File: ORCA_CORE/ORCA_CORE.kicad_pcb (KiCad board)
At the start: 4 copper layers, 73 x 134.1 mm, 184 parts, among them J1 data_line_power, J10 Raspberry_Pi_2_3, J11 I2C, J12 I2C, J13 6Vout, J15 Conn_01x05_Pin, J16 Conn_01x05_Pin, J17 Vin_motor, J18 data_line_power, J19 +5Vin_cpu, J2 I2C_power, J20 5Vout, J21 Conn_01x02, J3 Vout_motor, J4 emergence, J5 Vin_batt, J6 Vin_ex, J7 Vout_power2usp, J8 Vin_power2usp, J9 +5Vout_cpu, P1 USB_C_Receptacle_USB2.0, Q1 TJ60S04M3L, Q2 BSS138, Q3 BSS138, Q4 IRLML6402, Q5 TJ60S04M3L, Q6 BSS138, Q7 BSS138, Q8 BSS138, U1 LTC2301IMS, U10 HY2112, U11 AP64502, U12 TPS61230A__board, U13 FT230XS, U14 BNO055, U15 NJM78055DL1, U2 NJM78055DL1, U3 CN3058E, U4 RH1B-UDC6V, U5 TPH11006NL, U6 TPH11006NL, U7 NJW4860, U8 AZ1117-3.3, U9 FS8205

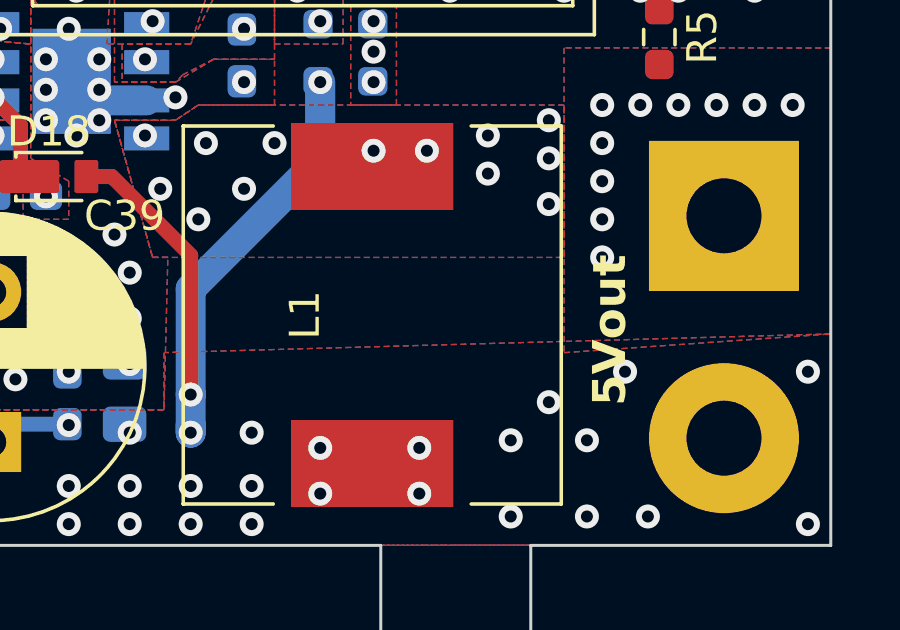
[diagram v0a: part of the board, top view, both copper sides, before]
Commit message: change extern lib path to project dir
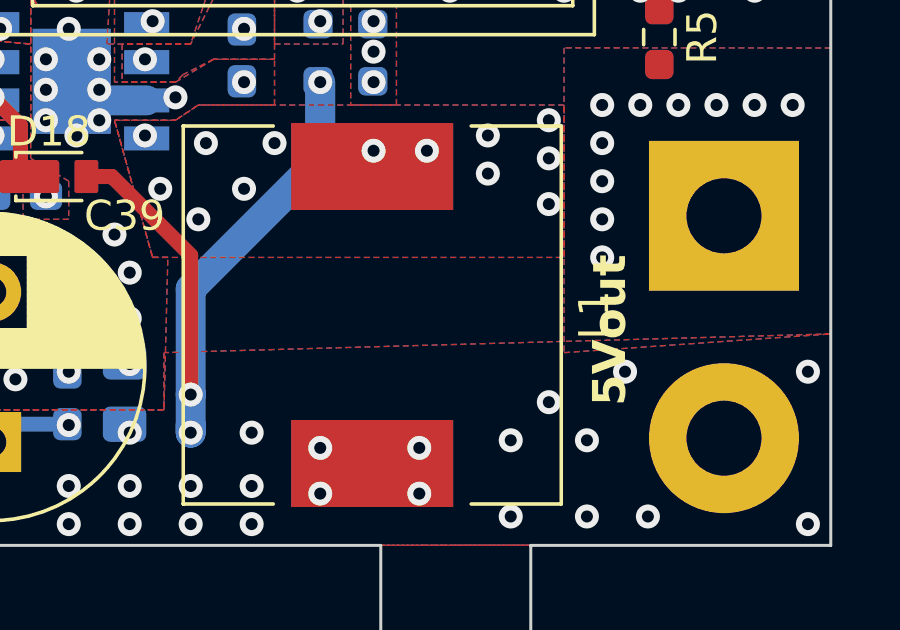
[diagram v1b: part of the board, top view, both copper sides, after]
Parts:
- L1: footprint Inductor_SMD:L_12x12mm_H8mm_withmodel -> inductor:L_12x12mm_H8mm_withmodel
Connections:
- D22 pad 2: GND2 -> Net-(D22-A)
- P1 pad A4: GND2 -> Net-(D22-A)
- P1 pad A9: GND2 -> Net-(D22-A)
- P1 pad B4: GND2 -> Net-(D22-A)
- P1 pad B9: GND2 -> Net-(D22-A)
- R40 pad 1: GND2 -> Net-(D22-A)

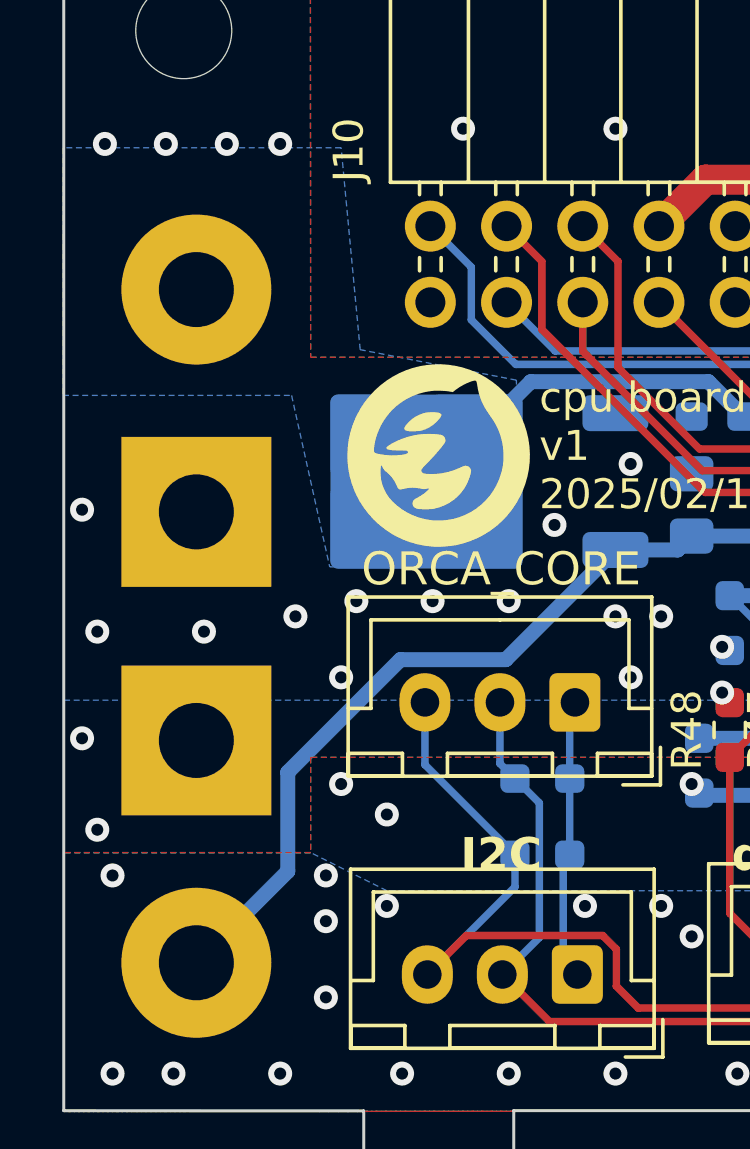
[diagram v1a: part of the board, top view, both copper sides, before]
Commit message: add silk screen
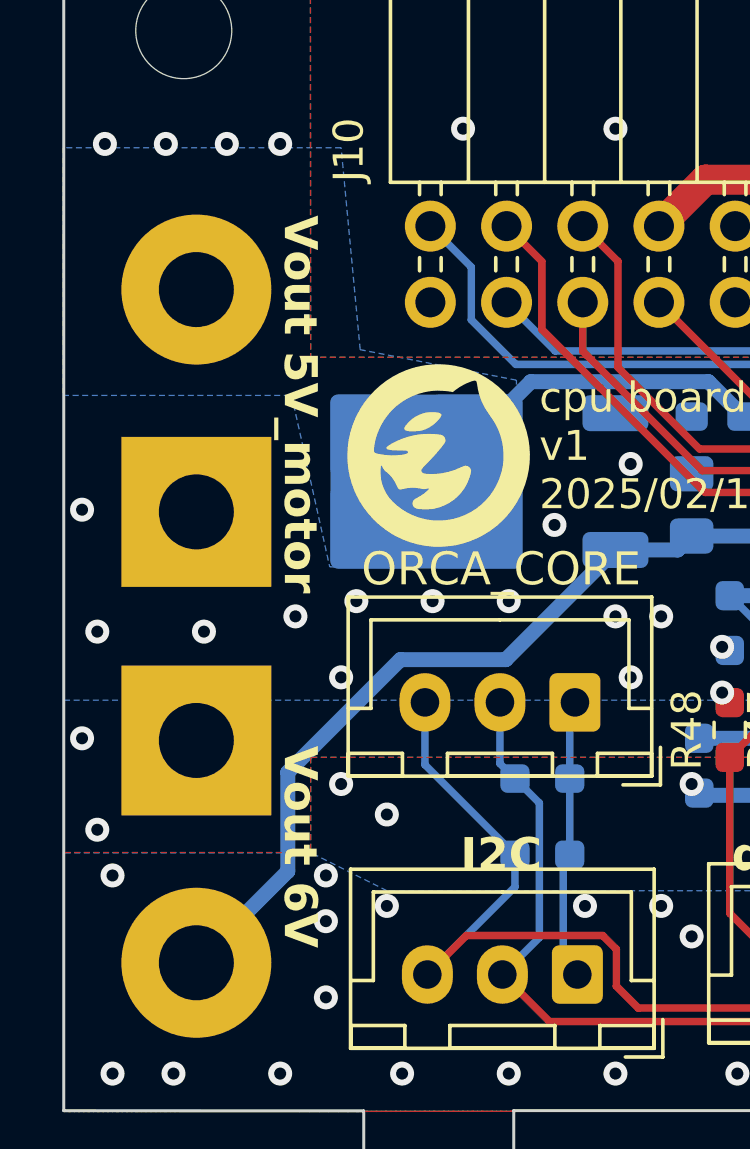
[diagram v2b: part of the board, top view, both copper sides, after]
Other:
- board text added: "Vout 5V_motor"
- board text added: "Vout 6V"

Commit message: solv errors
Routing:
- net Net-(D22-A): track 0.00 -> 30.4 mm, vias 0 -> 2
- net GND: track 46.7 -> 73.9 mm, vias 202 -> 211
- net GND2: track 132.4 -> 146.4 mm, vias 50 -> 49
- net +5V_cpu: track 50.7 -> 57.6 mm
- net reg_down_out: track 41.2 -> 43.1 mm
